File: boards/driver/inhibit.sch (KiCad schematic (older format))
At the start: 10 parts, among them Q58 MMBT2222, Q59 MMBT2222

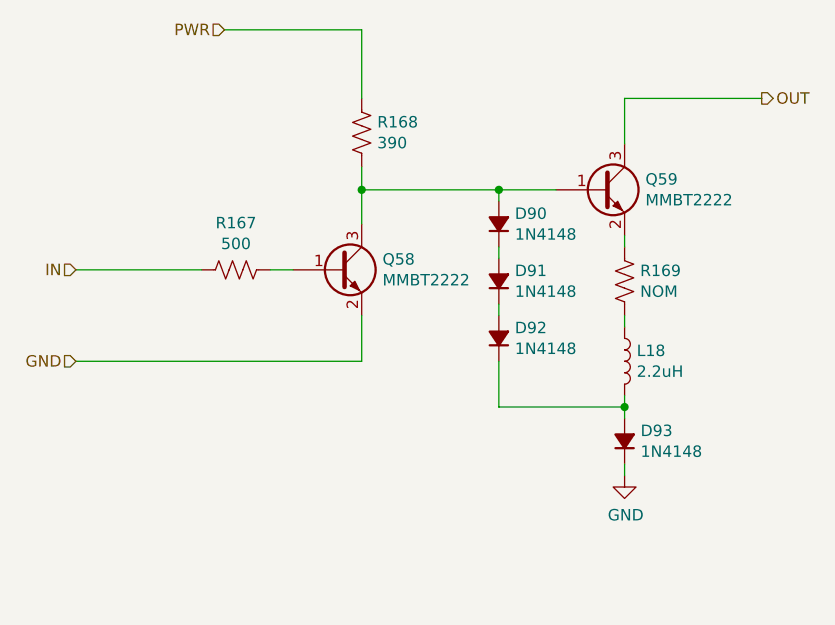
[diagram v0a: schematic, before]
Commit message: Driver board: a bit more schematic work and some initial footprint selections
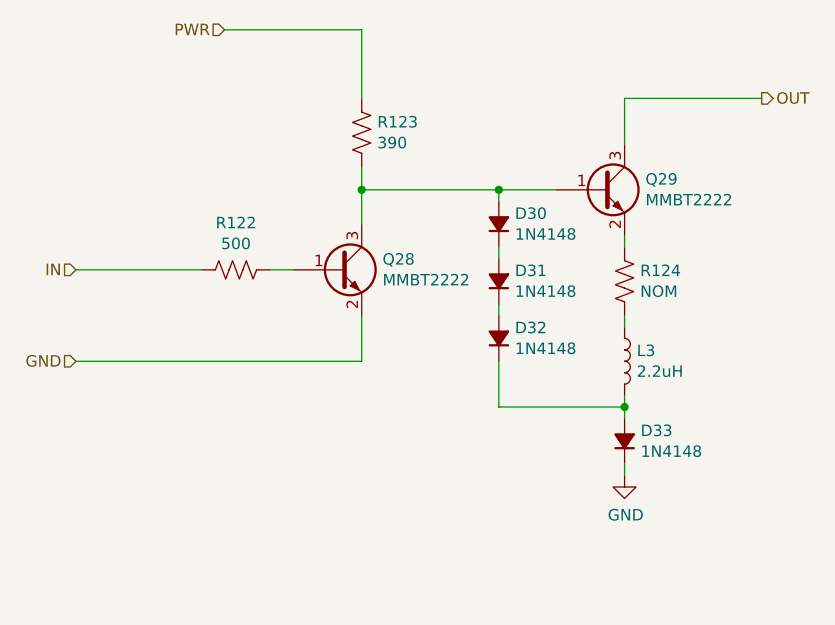
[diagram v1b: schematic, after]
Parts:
- R167, R168, R169: footprint Resistor_SMD:R_1206_3216Metric -> Resistor_SMD:R_0603_1608Metric
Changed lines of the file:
@@
 $Descr A4 11693 8268
 encoding utf-8
-Sheet 9 68
+Sheet 32 68
 Title ""
 Date ""
@@
 AR Path="/6183FAE6/624B82E8/62448373" Ref="R125"  Part="1"
 AR Path="/6183FAE6/624B82F7/62448373" Ref="R122"  Part="1"
-F 0 "R167" V 3445 3550 50  0000 C CNN
+F 0 "R122" V 3445 3550 50  0000 C CNN
 F 1 "500" V 3536 3550 50  0000 C CNN
-F 2 "Resistor_SMD:R_1206_3216Metric" V 3690 3540 50  0001 C CNN
+F 2 "Resistor_SMD:R_0603_1608Metric" V 3690 3540 50  0001 C CNN
 F 3 "~" H 3650 3550 50  0001 C CNN
 	1    3650 3550
@@
 AR Path="/6183FAE6/624B82E8/6244837A" Ref="Q30"  Part="1"
 AR Path="/6183FAE6/624B82F7/6244837A" Ref="Q28"  Part="1"
-F 0 "Q58" H 4291 3596 50  0000 L CNN
+F 0 "Q28" H 4291 3596 50  0000 L CNN
 F 1 "MMBT2222" H 4291 3505 50  0000 L CNN
 F 2 "Package_TO_SOT_SMD:SOT-23" H 4300 3650 50  0001 C CNN
@@
 AR Path="/6183FAE6/624B82E8/624483C4" Ref="D36"  Part="1"
 AR Path="/6183FAE6/624B82F7/624483C4" Ref="D32"  Part="1"
-F 0 "D92" V 4846 3780 50  0000 R CNN
+F 0 "D32" V 4846 3780 50  0000 R CNN
 F 1 "1N4148" V 4755 3780 50  0000 R CNN
 F 2 "Diode_SMD:D_SOD-323" V 4800 3850 50  0001 C CNN
@@
 AR Path="/6183FAE6/624B82E8/624483CA" Ref="D35"  Part="1"
 AR Path="/6183FAE6/624B82F7/624483CA" Ref="D31"  Part="1"
-F 0 "D91" V 4846 3530 50  0000 R CNN
+F 0 "D31" V 4846 3530 50  0000 R CNN
 F 1 "1N4148" V 4755 3530 50  0000 R CNN
 F 2 "Diode_SMD:D_SOD-323" V 4800 3600 50  0001 C CNN
@@
 AR Path="/6183FAE6/624B82E8/624483D0" Ref="D34"  Part="1"
 AR Path="/6183FAE6/624B82F7/624483D0" Ref="D30"  Part="1"
-F 0 "D90" V 4846 3280 50  0000 R CNN
+F 0 "D30" V 4846 3280 50  0000 R CNN
 F 1 "1N4148" V 4755 3280 50  0000 R CNN
 F 2 "Diode_SMD:D_SOD-323" V 4800 3350 50  0001 C CNN
@@
 AR Path="/6183FAE6/624B82E8/624483EF" Ref="#PWR063"  Part="1"
 AR Path="/6183FAE6/624B82F7/624483EF" Ref="#PWR062"  Part="1"
-F 0 "#PWR077" H 5350 4200 50  0001 C CNN
+F 0 "#PWR062" H 5350 4200 50  0001 C CNN
 F 1 "GND" H 5355 4277 50  0000 C CNN
 F 2 "" H 5350 4450 50  0001 C CNN
@@
 AR Path="/6183FAE6/624B82E8/624483F5" Ref="Q31"  Part="1"
 AR Path="/6183FAE6/624B82F7/624483F5" Ref="Q29"  Part="1"
-F 0 "Q59" H 5441 3246 50  0000 L CNN
+F 0 "Q29" H 5441 3246 50  0000 L CNN
 F 1 "MMBT2222" H 5441 3155 50  0000 L CNN
 F 2 "Package_TO_SOT_SMD:SOT-23" H 5450 3300 50  0001 C CNN
@@
 AR Path="/6183FAE6/624B82E8/62448410" Ref="R127"  Part="1"
 AR Path="/6183FAE6/624B82F7/62448410" Ref="R124"  Part="1"
-F 0 "R169" H 5418 3646 50  0000 L CNN
+F 0 "R124" H 5418 3646 50  0000 L CNN
 F 1 "NOM" H 5418 3555 50  0000 L CNN
-F 2 "Resistor_SMD:R_1206_3216Metric" V 5390 3590 50  0001 C CNN
+F 2 "Resistor_SMD:R_0603_1608Metric" V 5390 3590 50  0001 C CNN
 F 3 "~" H 5350 3600 50  0001 C CNN
 	1    5350 3600
@@
 AR Path="/6183FAE6/624B82E8/62448417" Ref="L4"  Part="1"
 AR Path="/6183FAE6/624B82F7/62448417" Ref="L3"  Part="1"
-F 0 "L18" H 5403 3996 50  0000 L CNN
+F 0 "L3" H 5403 3996 50  0000 L CNN
 F 1 "2.2uH" H 5403 3905 50  0000 L CNN
 F 2 "" H 5350 3950 50  0001 C CNN
@@
 AR Path="/6183FAE6/624B82E8/6245EF02" Ref="R126"  Part="1"
 AR Path="/6183FAE6/624B82F7/6245EF02" Ref="R123"  Part="1"
-F 0 "R168" H 4268 2996 50  0000 L CNN
+F 0 "R123" H 4268 2996 50  0000 L CNN
 F 1 "390" H 4268 2905 50  0000 L CNN
-F 2 "Resistor_SMD:R_1206_3216Metric" V 4240 2940 50  0001 C CNN
+F 2 "Resistor_SMD:R_0603_1608Metric" V 4240 2940 50  0001 C CNN
 F 3 "~" H 4200 2950 50  0001 C CNN
 	1    4200 2950
@@
 AR Path="/6183FAE6/624B82E8/624611F8" Ref="D37"  Part="1"
 AR Path="/6183FAE6/624B82F7/624611F8" Ref="D33"  Part="1"
-F 0 "D93" V 5396 4230 50  0000 R CNN
+F 0 "D33" V 5396 4230 50  0000 R CNN
 F 1 "1N4148" V 5305 4230 50  0000 R CNN
 F 2 "Diode_SMD:D_SOD-323" V 5350 4300 50  0001 C CNN

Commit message: Driver board: finished first rough draft schematic. Lots of placeholders, but at least every place is held.
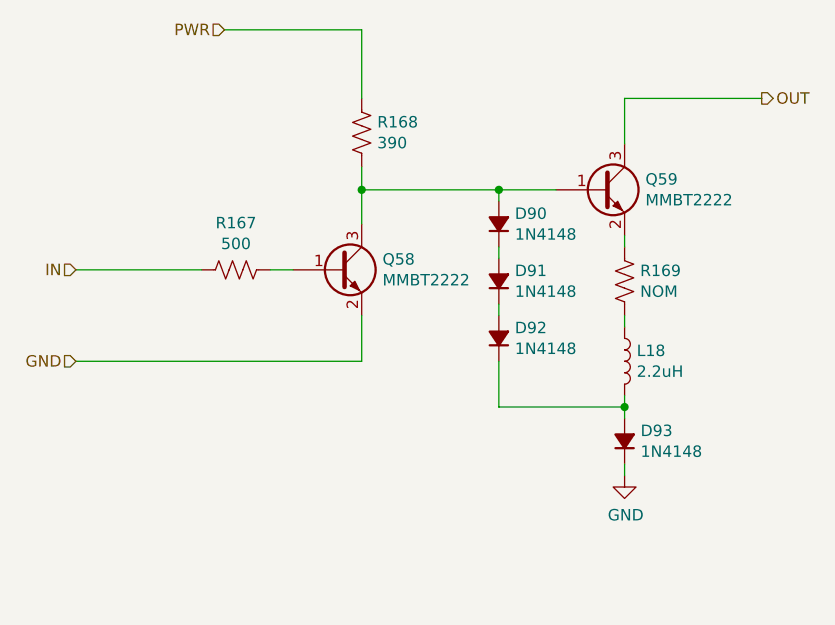
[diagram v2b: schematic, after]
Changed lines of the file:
@@
 $Descr A4 11693 8268
 encoding utf-8
-Sheet 32 68
+Sheet 32 69
 Title ""
 Date ""
@@
 AR Path="/6183FAE6/624B82E8/62448373" Ref="R125"  Part="1"
 AR Path="/6183FAE6/624B82F7/62448373" Ref="R122"  Part="1"
-F 0 "R122" V 3445 3550 50  0000 C CNN
+F 0 "R167" V 3445 3550 50  0000 C CNN
 F 1 "500" V 3536 3550 50  0000 C CNN
 F 2 "Resistor_SMD:R_0603_1608Metric" V 3690 3540 50  0001 C CNN
@@
 AR Path="/6183FAE6/624B82E8/6244837A" Ref="Q30"  Part="1"
 AR Path="/6183FAE6/624B82F7/6244837A" Ref="Q28"  Part="1"
-F 0 "Q28" H 4291 3596 50  0000 L CNN
+F 0 "Q58" H 4291 3596 50  0000 L CNN
 F 1 "MMBT2222" H 4291 3505 50  0000 L CNN
 F 2 "Package_TO_SOT_SMD:SOT-23" H 4300 3650 50  0001 C CNN
@@
 AR Path="/6183FAE6/624B82E8/624483C4" Ref="D36"  Part="1"
 AR Path="/6183FAE6/624B82F7/624483C4" Ref="D32"  Part="1"
-F 0 "D32" V 4846 3780 50  0000 R CNN
+F 0 "D92" V 4846 3780 50  0000 R CNN
 F 1 "1N4148" V 4755 3780 50  0000 R CNN
 F 2 "Diode_SMD:D_SOD-323" V 4800 3850 50  0001 C CNN
@@
 AR Path="/6183FAE6/624B82E8/624483CA" Ref="D35"  Part="1"
 AR Path="/6183FAE6/624B82F7/624483CA" Ref="D31"  Part="1"
-F 0 "D31" V 4846 3530 50  0000 R CNN
+F 0 "D91" V 4846 3530 50  0000 R CNN
 F 1 "1N4148" V 4755 3530 50  0000 R CNN
 F 2 "Diode_SMD:D_SOD-323" V 4800 3600 50  0001 C CNN
@@
 AR Path="/6183FAE6/624B82E8/624483D0" Ref="D34"  Part="1"
 AR Path="/6183FAE6/624B82F7/624483D0" Ref="D30"  Part="1"
-F 0 "D30" V 4846 3280 50  0000 R CNN
+F 0 "D90" V 4846 3280 50  0000 R CNN
 F 1 "1N4148" V 4755 3280 50  0000 R CNN
 F 2 "Diode_SMD:D_SOD-323" V 4800 3350 50  0001 C CNN
@@
 AR Path="/6183FAE6/624B82E8/624483EF" Ref="#PWR063"  Part="1"
 AR Path="/6183FAE6/624B82F7/624483EF" Ref="#PWR062"  Part="1"
-F 0 "#PWR062" H 5350 4200 50  0001 C CNN
+F 0 "#PWR077" H 5350 4200 50  0001 C CNN
 F 1 "GND" H 5355 4277 50  0000 C CNN
 F 2 "" H 5350 4450 50  0001 C CNN
@@
 AR Path="/6183FAE6/624B82E8/624483F5" Ref="Q31"  Part="1"
 AR Path="/6183FAE6/624B82F7/624483F5" Ref="Q29"  Part="1"
-F 0 "Q29" H 5441 3246 50  0000 L CNN
+F 0 "Q59" H 5441 3246 50  0000 L CNN
 F 1 "MMBT2222" H 5441 3155 50  0000 L CNN
 F 2 "Package_TO_SOT_SMD:SOT-23" H 5450 3300 50  0001 C CNN
@@
 AR Path="/6183FAE6/624B82E8/62448410" Ref="R127"  Part="1"
 AR Path="/6183FAE6/624B82F7/62448410" Ref="R124"  Part="1"
-F 0 "R124" H 5418 3646 50  0000 L CNN
+F 0 "R169" H 5418 3646 50  0000 L CNN
 F 1 "NOM" H 5418 3555 50  0000 L CNN
 F 2 "Resistor_SMD:R_0603_1608Metric" V 5390 3590 50  0001 C CNN
@@
 AR Path="/6183FAE6/624B82E8/62448417" Ref="L4"  Part="1"
 AR Path="/6183FAE6/624B82F7/62448417" Ref="L3"  Part="1"
-F 0 "L3" H 5403 3996 50  0000 L CNN
+F 0 "L18" H 5403 3996 50  0000 L CNN
 F 1 "2.2uH" H 5403 3905 50  0000 L CNN
 F 2 "" H 5350 3950 50  0001 C CNN
@@
 AR Path="/6183FAE6/624B82E8/6245EF02" Ref="R126"  Part="1"
 AR Path="/6183FAE6/624B82F7/6245EF02" Ref="R123"  Part="1"
-F 0 "R123" H 4268 2996 50  0000 L CNN
+F 0 "R168" H 4268 2996 50  0000 L CNN
 F 1 "390" H 4268 2905 50  0000 L CNN
 F 2 "Resistor_SMD:R_0603_1608Metric" V 4240 2940 50  0001 C CNN
@@
 AR Path="/6183FAE6/624B82E8/624611F8" Ref="D37"  Part="1"
 AR Path="/6183FAE6/624B82F7/624611F8" Ref="D33"  Part="1"
-F 0 "D33" V 5396 4230 50  0000 R CNN
+F 0 "D93" V 5396 4230 50  0000 R CNN
 F 1 "1N4148" V 5305 4230 50  0000 R CNN
 F 2 "Diode_SMD:D_SOD-323" V 5350 4300 50  0001 C CNN

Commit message: Driver board: fleshed out the hotswap controller, tweaked some resistors, and added some bypass caps
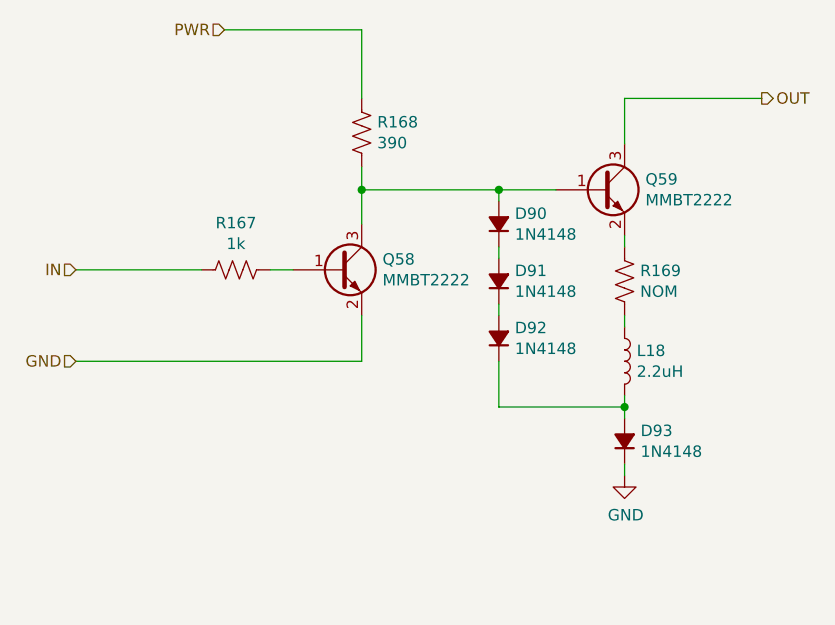
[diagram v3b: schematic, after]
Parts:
- R167: value 500 -> 1k
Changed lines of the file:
@@
 $Descr A4 11693 8268
 encoding utf-8
-Sheet 32 69
+Sheet 47 69
 Title ""
 Date ""
@@
 AR Path="/6183FAE6/624B82F7/62448373" Ref="R122"  Part="1"
 F 0 "R167" V 3445 3550 50  0000 C CNN
-F 1 "500" V 3536 3550 50  0000 C CNN
+F 1 "1k" V 3536 3550 50  0000 C CNN
 F 2 "Resistor_SMD:R_0603_1608Metric" V 3690 3540 50  0001 C CNN
 F 3 "~" H 3650 3550 50  0001 C CNN
@@
 AR Path="/6183FAE6/623E7DB1/624483EF" Ref="#PWR?"  Part="1"
 AR Path="/6183FAE6/623E7DC0/624483EF" Ref="#PWR?"  Part="1"
-AR Path="/6183FAE6/62442CC1/624483EF" Ref="#PWR077"  Part="1"
-AR Path="/6183FAE6/62464AF7/624483EF" Ref="#PWR076"  Part="1"
-AR Path="/6183FAE6/6247B051/624483EF" Ref="#PWR075"  Part="1"
-AR Path="/6183FAE6/6247B057/624483EF" Ref="#PWR074"  Part="1"
-AR Path="/6183FAE6/62482DEF/624483EF" Ref="#PWR073"  Part="1"
-AR Path="/6183FAE6/62482DF5/624483EF" Ref="#PWR072"  Part="1"
-AR Path="/6183FAE6/62482E09/624483EF" Ref="#PWR071"  Part="1"
+AR Path="/6183FAE6/62442CC1/624483EF" Ref="#PWR080"  Part="1"
+AR Path="/6183FAE6/62464AF7/624483EF" Ref="#PWR079"  Part="1"
+AR Path="/6183FAE6/6247B051/624483EF" Ref="#PWR078"  Part="1"
+AR Path="/6183FAE6/6247B057/624483EF" Ref="#PWR077"  Part="1"
+AR Path="/6183FAE6/62482DEF/624483EF" Ref="#PWR076"  Part="1"
+AR Path="/6183FAE6/62482DF5/624483EF" Ref="#PWR075"  Part="1"
+AR Path="/6183FAE6/62482E09/624483EF" Ref="#PWR074"  Part="1"
 AR Path="/6183FAE6/62482E0F/624483EF" Ref="#PWR?"  Part="1"
-AR Path="/6183FAE6/62495C8E/624483EF" Ref="#PWR070"  Part="1"
-AR Path="/6183FAE6/624B829C/624483EF" Ref="#PWR069"  Part="1"
-AR Path="/6183FAE6/624B82A2/624483EF" Ref="#PWR068"  Part="1"
-AR Path="/6183FAE6/624B82B6/624483EF" Ref="#PWR067"  Part="1"
-AR Path="/6183FAE6/624B82BC/624483EF" Ref="#PWR066"  Part="1"
-AR Path="/6183FAE6/624B82D0/624483EF" Ref="#PWR065"  Part="1"
-AR Path="/6183FAE6/624B82D6/624483EF" Ref="#PWR064"  Part="1"
-AR Path="/6183FAE6/624B82E8/624483EF" Ref="#PWR063"  Part="1"
-AR Path="/6183FAE6/624B82F7/624483EF" Ref="#PWR062"  Part="1"
-F 0 "#PWR077" H 5350 4200 50  0001 C CNN
+AR Path="/6183FAE6/62495C8E/624483EF" Ref="#PWR073"  Part="1"
+AR Path="/6183FAE6/624B829C/624483EF" Ref="#PWR072"  Part="1"
+AR Path="/6183FAE6/624B82A2/624483EF" Ref="#PWR071"  Part="1"
+AR Path="/6183FAE6/624B82B6/624483EF" Ref="#PWR070"  Part="1"
+AR Path="/6183FAE6/624B82BC/624483EF" Ref="#PWR069"  Part="1"
+AR Path="/6183FAE6/624B82D0/624483EF" Ref="#PWR068"  Part="1"
+AR Path="/6183FAE6/624B82D6/624483EF" Ref="#PWR067"  Part="1"
+AR Path="/6183FAE6/624B82E8/624483EF" Ref="#PWR066"  Part="1"
+AR Path="/6183FAE6/624B82F7/624483EF" Ref="#PWR065"  Part="1"
+F 0 "#PWR080" H 5350 4200 50  0001 C CNN
 F 1 "GND" H 5355 4277 50  0000 C CNN
 F 2 "" H 5350 4450 50  0001 C CNN

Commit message: Driver board: significant cleanup. Moved sense amp pairs into a subsheet, split tuning resistors into two globally, pushed input circuits into their corresponding sheets.
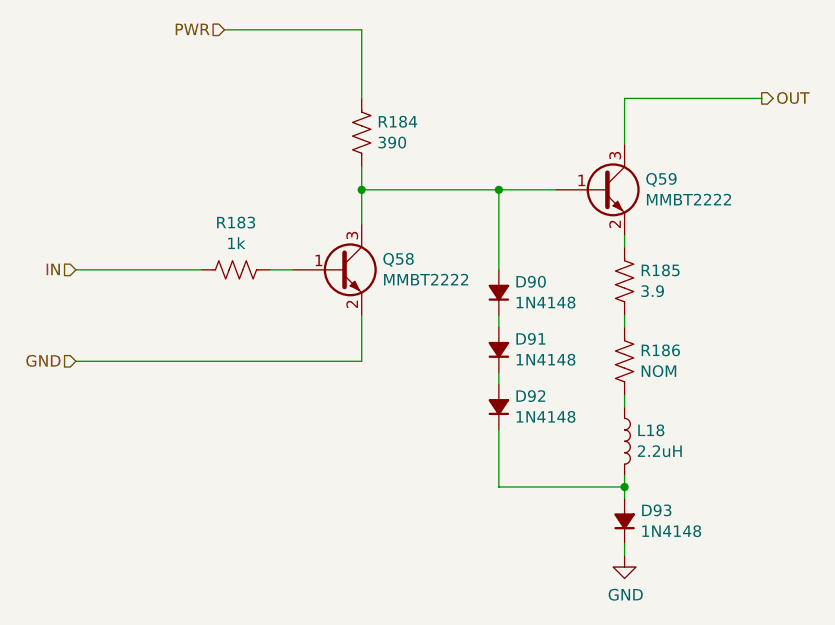
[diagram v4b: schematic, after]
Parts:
- added R186: NOM, Resistor_SMD:R_0603_1608Metric, symbol Device:R_US
- L18: footprint (none) -> Inductor_SMD:L_1812_4532Metric
- R185: renamed from R169; value NOM -> 3.9
- renumbered R167 to R183, R168 to R184
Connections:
- net at R185.2: now also R186.1; no longer L18.1
- new net: L18.1, R186.2
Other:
- moved on the sheet: D90, D91, D92, D93, L18

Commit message: Driver board: integrated DIN 41612 backplane connector, and made a dedicated parity inhibit sheet with a different set resistor value.
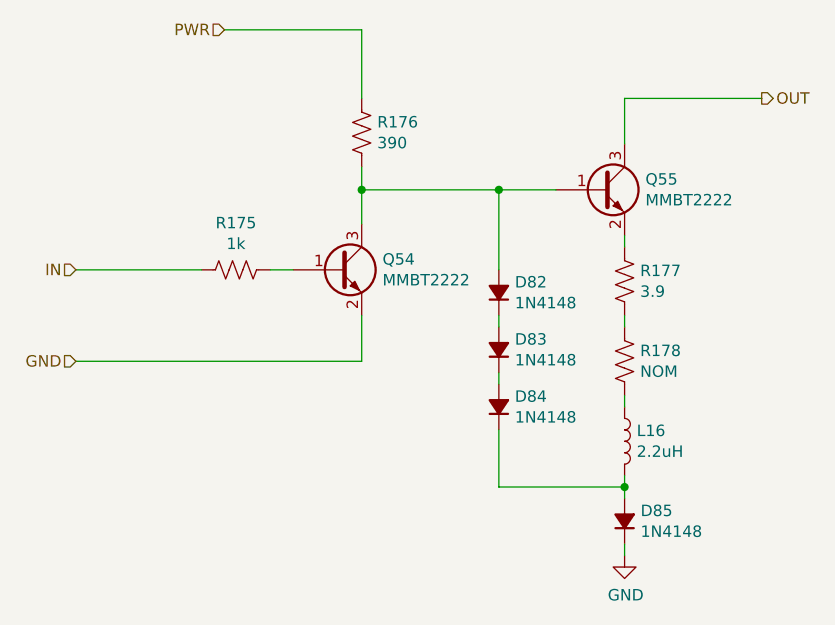
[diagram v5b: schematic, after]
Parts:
- renumbered D90 to D82, D91 to D83, D92 to D84, D93 to D85, L18 to L16, Q58 to Q54, Q59 to Q55, R183 to R175, R184 to R176, R185 to R177, R186 to R178

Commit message: Driver board: largely fleshed out part selection
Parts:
- D82, D83, D84, D85: Digikey (none) -> https://www.digikey.com/en/products/detail/smc-diode-soluti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; Part Number (none) -> 1N4148WSTR
- L16: DCR (none) -> 0.7; Digikey (none) -> https://www.digikey.com/en/products/detail/api-delevan-inc/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; Part Number (none) -> 1812R-222J; Rating (none) -> 535mA; Tolerance (none) -> 5%
- Q54, Q55: Digikey (none) -> https://www.digikey.com/en/products/detail/MMBT2222A-G/641-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; Part Number (none) -> MMBT2222A-G
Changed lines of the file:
@@
 $Descr A4 11693 8268
 encoding utf-8
-Sheet 34 64
+Sheet 40 64
 Title ""
 Date ""
@@
 F 2 "Package_TO_SOT_SMD:SOT-23" H 4300 3650 50  0001 C CNN
 F 3 "~" H 4100 3550 50  0001 C CNN
+F 4 "https://www.digikey.com/en/products/detail/MMBT2222A-G/641-1942-1-ND/9477875" H 4100 3550 50  0001 C CNN "Digikey"
+F 5 "MMBT2222A-G" H 4100 3550 50  0001 C CNN "Part Number"
 	1    4100 3550
 	1    0    0    -1
@@
 F 2 "Diode_SMD:D_SOD-323" V 4800 4150 50  0001 C CNN
 F 3 "~" V 4800 4150 50  0001 C CNN
+F 4 "1N4148WSTR" V 4900 3150 50  0001 C CNN "Part Number"
+F 5 "https://www.digikey.com/en/products/detail/smc-diode-solutions/1N4148WSTR/6022449" V 4900 3150 50  0001 C CNN "Digikey"
 	1    4800 4150
 	0    -1   -1   0
@@
 F 2 "Diode_SMD:D_SOD-323" V 4800 3900 50  0001 C CNN
 F 3 "~" V 4800 3900 50  0001 C CNN
+F 4 "1N4148WSTR" V 4900 3150 50  0001 C CNN "Part Number"
+F 5 "https://www.digikey.com/en/products/detail/smc-diode-solutions/1N4148WSTR/6022449" V 4900 3150 50  0001 C CNN "Digikey"
 	1    4800 3900
 	0    -1   -1   0
@@
 F 2 "Diode_SMD:D_SOD-323" V 4800 3650 50  0001 C CNN
 F 3 "~" V 4800 3650 50  0001 C CNN
+F 4 "1N4148WSTR" V 4900 3150 50  0001 C CNN "Part Number"
+F 5 "https://www.digikey.com/en/products/detail/smc-diode-solutions/1N4148WSTR/6022449" V 4900 3150 50  0001 C CNN "Digikey"
 	1    4800 3650
 	0    -1   -1   0
@@
 F 2 "Package_TO_SOT_SMD:SOT-23" H 5450 3300 50  0001 C CNN
 F 3 "~" H 5250 3200 50  0001 C CNN
+F 4 "https://www.digikey.com/en/products/detail/MMBT2222A-G/641-1942-1-ND/9477875" H 5250 3200 50  0001 C CNN "Digikey"
+F 5 "MMBT2222A-G" H 5250 3200 50  0001 C CNN "Part Number"
 	1    5250 3200
 	1    0    0    -1
@@
 F 2 "Diode_SMD:D_SOD-323" V 5350 4650 50  0001 C CNN
 F 3 "~" V 5350 4650 50  0001 C CNN
+F 4 "1N4148WSTR" V 4900 3150 50  0001 C CNN "Part Number"
+F 5 "https://www.digikey.com/en/products/detail/smc-diode-solutions/1N4148WSTR/6022449" V 4900 3150 50  0001 C CNN "Digikey"
 	1    5350 4650
 	0    -1   -1   0
@@
 F 2 "Inductor_SMD:L_1812_4532Metric" H 5350 4300 50  0001 C CNN
 F 3 "~" H 5350 4300 50  0001 C CNN
+F 4 "0.7" H 5350 4300 50  0001 C CNN "DCR"
+F 5 "https://www.digikey.com/en/products/detail/api-delevan-inc/1812R-222J/1115305" H 5350 4300 50  0001 C CNN "Digikey"
+F 6 "1812R-222J" H 5350 4300 50  0001 C CNN "Part Number"
+F 7 "535mA" H 5350 4300 50  0001 C CNN "Rating"
+F 8 "5%" H 5350 4300 50  0001 C CNN "Tolerance"
 	1    5350 4300
 	1    0    0    -1
